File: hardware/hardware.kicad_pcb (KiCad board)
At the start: 4 copper layers, 72 x 100 mm, 48 parts, among them J1 USB_B_Micro, J10 Conn_01x05_Pin, J11 Conn_01x04_Pin, J12 Conn_02x04_Odd_Even, J2 Conn_Coaxial, J3 Conn_01x03, J4 Conn_01x03, J5 Conn_01x03, J6 Conn_01x03, J7 Conn_01x02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

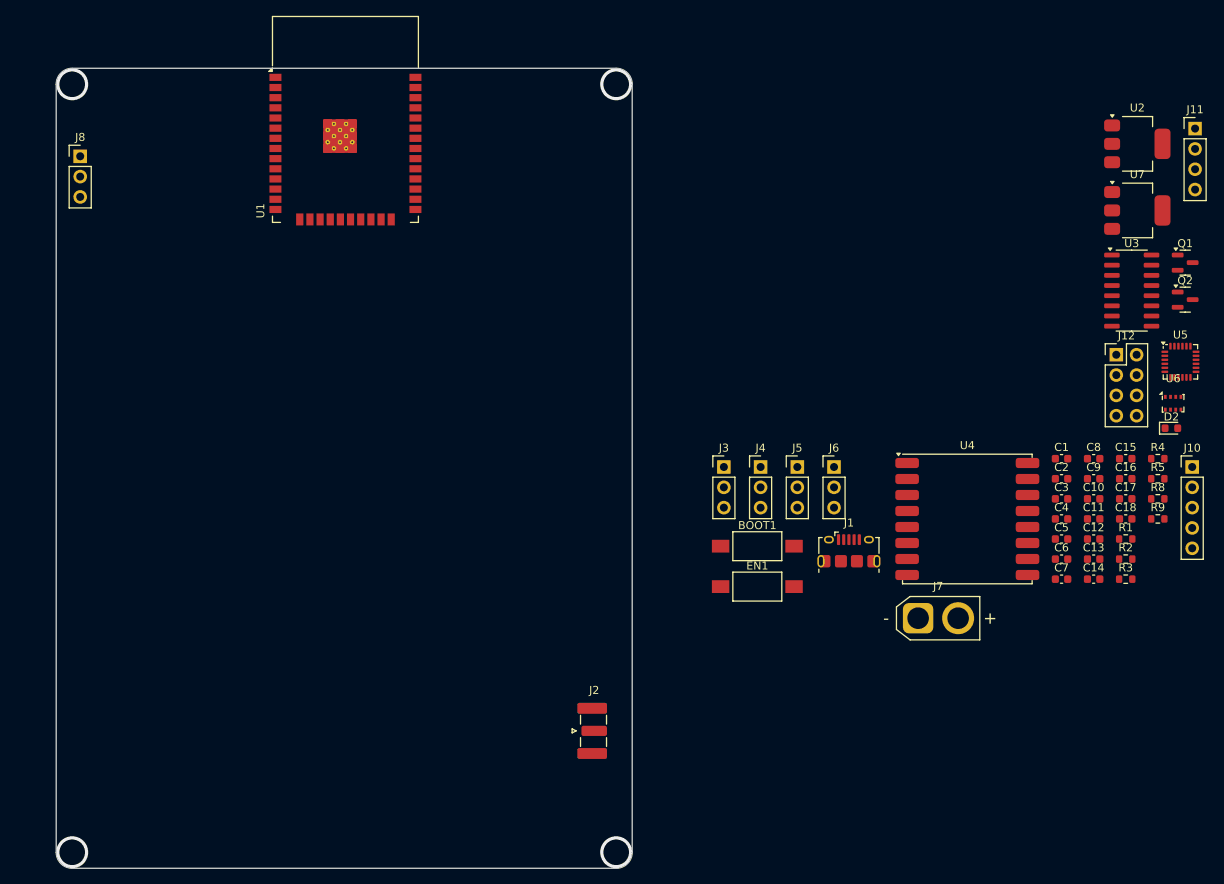
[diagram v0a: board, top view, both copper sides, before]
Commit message: update wiring
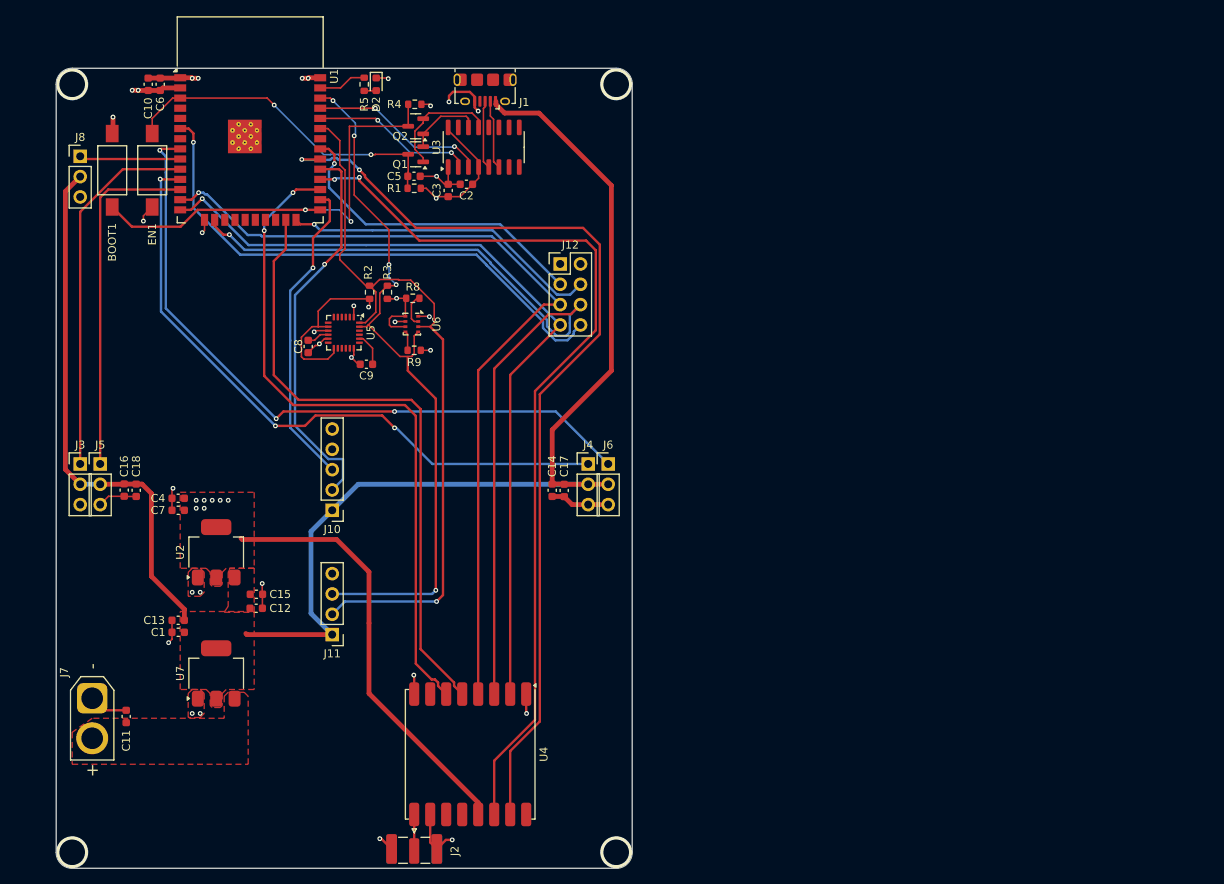
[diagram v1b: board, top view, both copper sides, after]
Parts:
- moved C10 129.0 mm to (104.5, 32.0), turned to 90 degrees
- moved U7 128.9 mm to (113.0, 105.7), turned to 90 degrees
- moved C6 127.3 mm to (106.0, 32.0), turned to 90 degrees
- moved U2 126.0 mm to (113.0, 90.5), turned to 90 degrees
- moved C16 125.2 mm to (101.5, 82.7), turned to -90 degrees
- moved J11 125.0 mm to (127.5, 100.8), turned to 180 degrees
- moved C18 123.7 mm to (103.0, 82.8), turned to -90 degrees
- moved C11 123.4 mm to (101.8, 111.0), turned to 90 degrees
- moved C13 114.7 mm to (108.2, 99.0), turned to 180 degrees
- moved C1 112.5 mm to (108.2, 100.5), turned to 180 degrees
- moved R5 110.8 mm to (131.5, 32.0), turned to -90 degrees
- moved C7 110.8 mm to (108.2, 85.2)
- moved C4 110.5 mm to (108.2, 83.8), turned to 180 degrees
- moved C15 110.0 mm to (118.0, 95.8)
- moved D2 108.3 mm to (133.0, 32.0), turned to -90 degrees
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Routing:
- net +5V: track 0.00 -> 195.3 mm
- net DIO1: track 0.00 -> 120.2 mm, vias 0 -> 2
- net DIO0: track 0.00 -> 114.4 mm, vias 0 -> 2
- net MOSI: track 0.00 -> 110.4 mm, vias 0 -> 1
- net +3V3: track 0.00 -> 109.1 mm, vias 0 -> 13
- net SCLK: track 0.00 -> 107.8 mm, vias 0 -> 1
- net MISO: track 0.00 -> 103.3 mm, vias 0 -> 1
- net SDA: track 0.00 -> 93.1 mm, vias 0 -> 1
- net SCL: track 0.00 -> 90.6 mm, vias 0 -> 5
- net GND: track 0.00 -> 87.7 mm, vias 4 -> 33
- net SR4: track 0.00 -> 86.8 mm, vias 0 -> 3
- net LORA_RST: track 0.00 -> 85.6 mm, vias 0 -> 2
- net SR2: track 0.00 -> 81.5 mm, vias 0 -> 3
- net SS: track 0.00 -> 77.9 mm
- net NRF_IRQ: track 0.00 -> 67.9 mm, vias 0 -> 1
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- added copper zone on F.Cu, net +3V3
- added copper zone on F.Cu, net +5V
- added copper zone on F.Cu, net +BATT
- added copper zone on F.Cu, net GND

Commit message: add battery fix
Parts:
- moved J4 1.10 mm to (158.4, 79.5)
- moved J5 1.10 mm to (99.6, 79.5)
- moved C14 0.74 mm to (154.3, 82.8)
- moved C17 0.74 mm to (155.8, 82.8)
- moved C16 0.74 mm to (102.2, 82.7)
- moved C18 0.74 mm to (103.7, 82.8)
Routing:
- net GND: track 87.7 -> 85.0 mm
- net LORA_RST: track 85.6 -> 84.7 mm
- net SS: track 77.9 -> 77.1 mm
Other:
- board size 72 x 100 mm -> 82 x 100 mm
